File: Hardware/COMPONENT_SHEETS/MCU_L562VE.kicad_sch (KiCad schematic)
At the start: 31 parts, among them SW1 MCU Reset, U2 STM32L562VET6Q, Y1 32MHz

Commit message: Routed Alert I2C lines
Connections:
- net I2C2_EN: now reaches U2.43 (PE15)
- no-connect marks 59 -> 58
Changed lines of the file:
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@@
   (no_connect (at 77.47 60.96))
   (no_connect (at 77.47 119.38))
-  (no_connect (at 77.47 121.92))
   (no_connect (at 123.19 162.56))
   (no_connect (at 77.47 48.26))
@@
   (no_connect (at 123.19 88.9))
   (no_connect (at 123.19 83.82))
+  (no_connect (at 77.47 111.76))
   (no_connect (at 77.47 104.14))
   (no_connect (at 77.47 106.68))
   (no_connect (at 77.47 109.22))
-  (no_connect (at 77.47 111.76))
   (no_connect (at 123.19 50.8))
   (no_connect (at 123.19 93.98))
@@
     (effects (font (size 1.27 1.27)) (justify left))
   )
+  (hierarchical_label "I2C2_EN" (shape input) (at 77.47 121.92 180)
+    (effects (font (size 1.27 1.27)) (justify right))
+  )
   (hierarchical_label "ABORT_2" (shape input) (at 123.19 106.68 0)

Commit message: All traces routed
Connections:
- net at U2.38 (PE10): now also D1.2 (A)
- net at U2.39 (PE11): now also D2.2 (A)
- net at U2.40 (PE12): now also D3.2 (A)
- net at U2.41 (PE13): now also D4.2 (A)
- net at U2.42 (PE14): now also D5.2 (A)
- no-connect marks 58 -> 53
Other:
- moved on the sheet: D1, D2, D3, D4, D5, R17, R18, R19, R20, R21

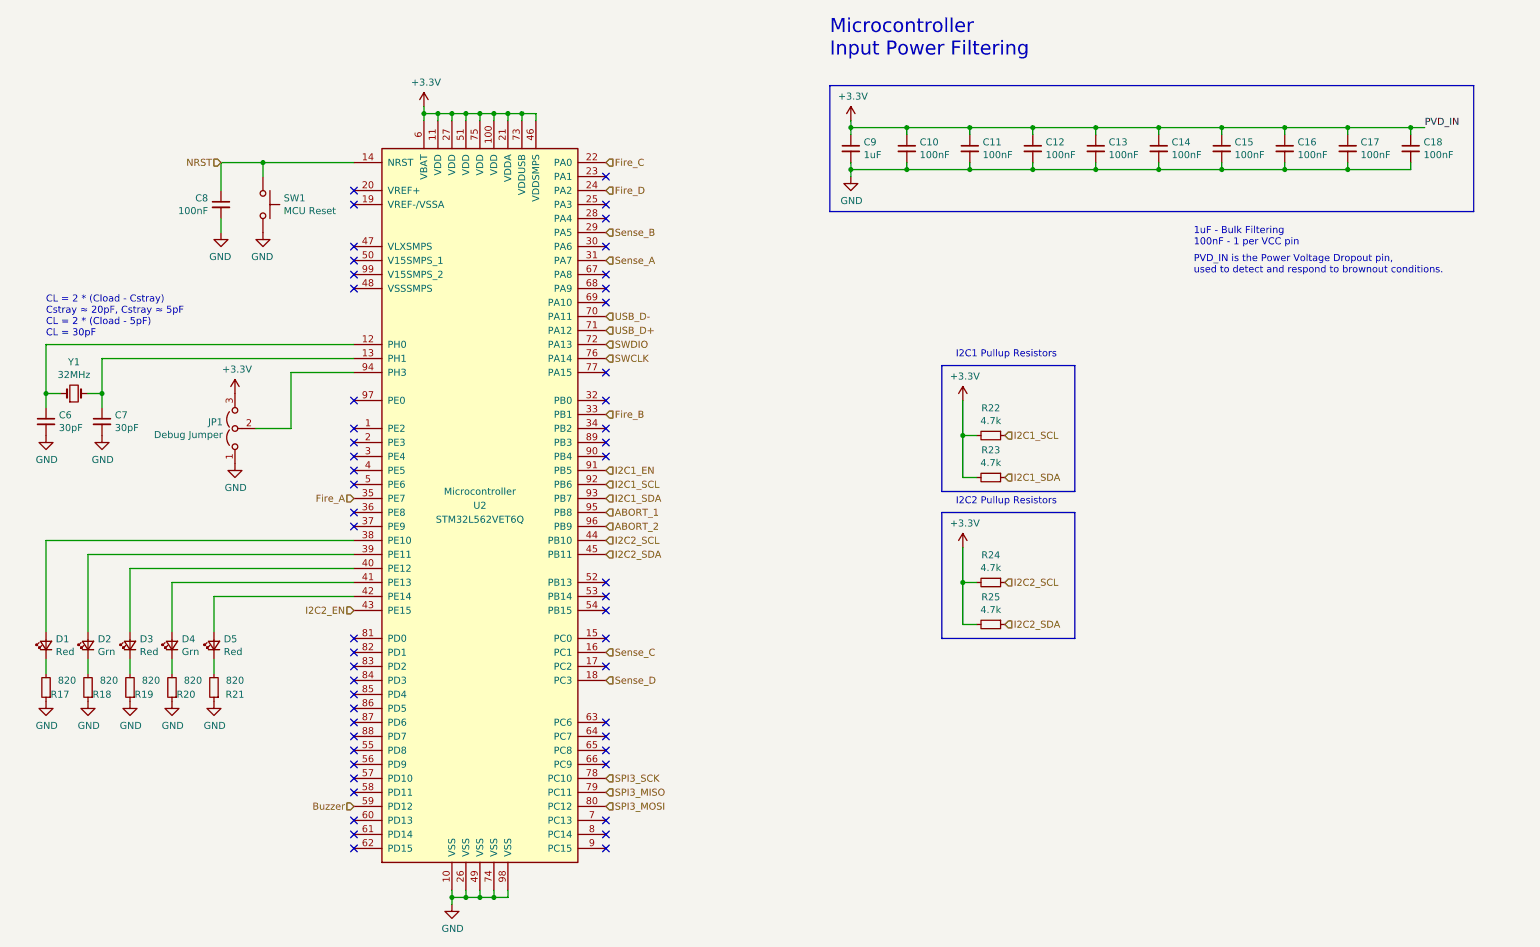
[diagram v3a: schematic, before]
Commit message: Adjusted silkscreen labels, corrected MCU pinout, added pull up resistor to bootloader line, added usb cut out
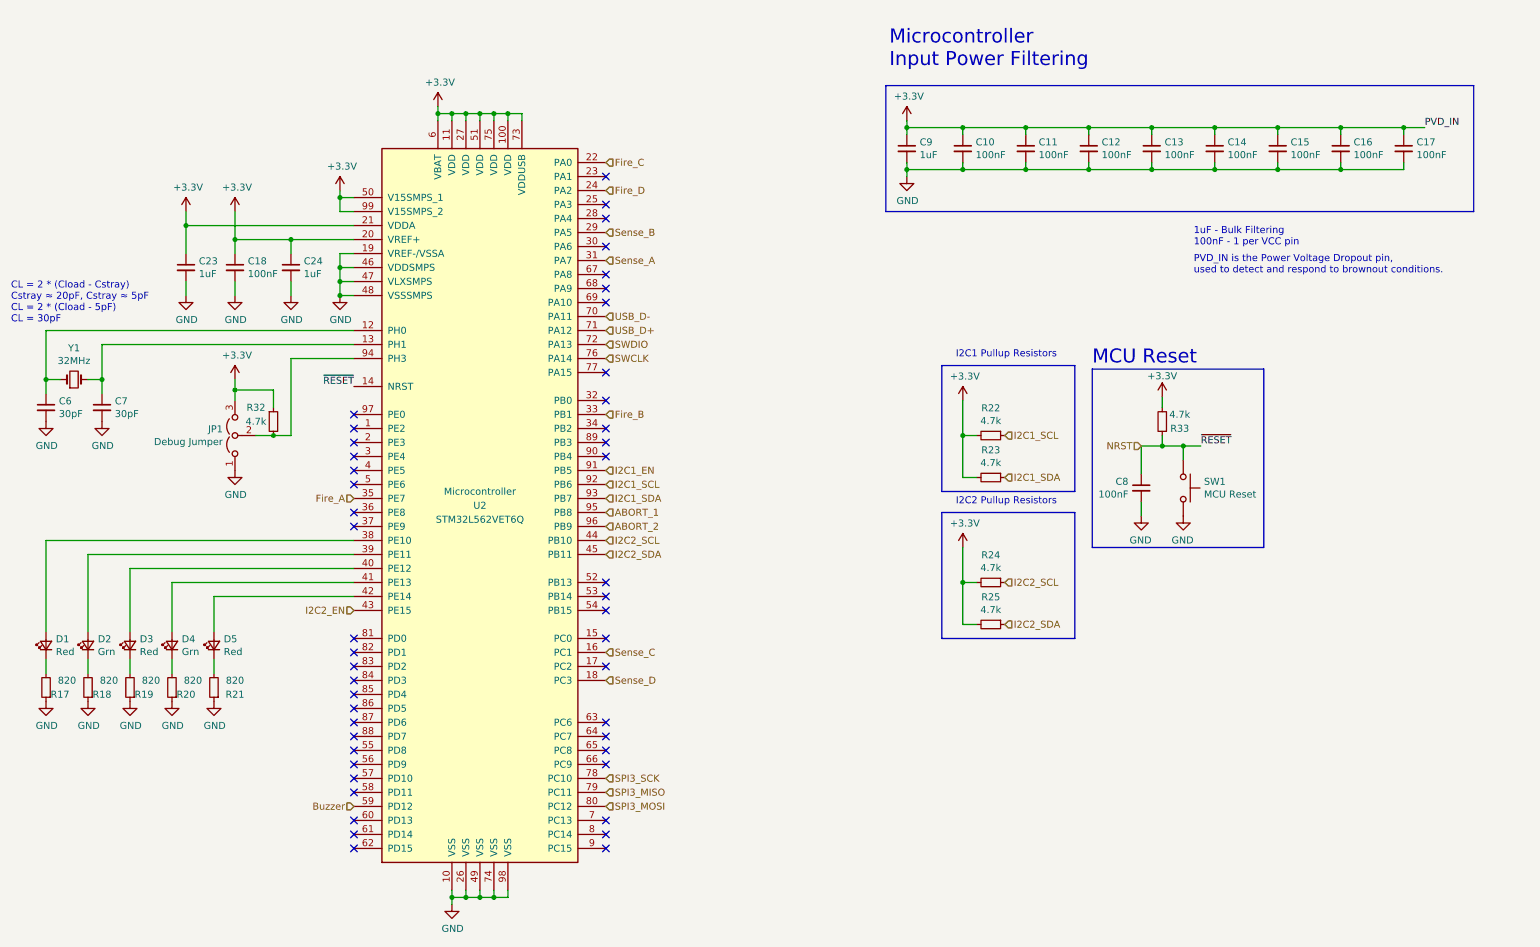
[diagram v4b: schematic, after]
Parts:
- added C23, C24: 1uF, Capacitor_SMD:C_0603_1608Metric_Pad1.08x0.95mm_HandSolder, symbol Device:C_Small
- added R32: 4.7k, Resistor_SMD:R_0603_1608Metric_Pad0.98x0.95mm_HandSolder, symbol Device:R_Small
- added R33: 4.7k, Resistor_SMD:R_0603_1608Metric_Pad1.05x0.95mm_HandSolder, symbol Device:R_Small
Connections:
- net +3V3: now also U2.20 (VREF+), U2.50 (V15SMPS_1), U2.99 (V15SMPS_2), C23.1, C24.1, R32.1, R33.2; no longer U2.46 (VDDSMPS)
- net GND: now also U2.19 (VREF-/VSSA), U2.46 (VDDSMPS), U2.47 (VLXSMPS), U2.48 (VSSSMPS), C23.2, C24.2
- net NRST: now also R33.1
- net at JP1.2 (C), U2.94 (PH3): now also R32.2
- no-connect marks 53 -> 47
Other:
- note added: "MCU Reset"
- moved on the sheet: C10, C11, C12, C13, C14, C15, C16, C17, C6, C7, C9, JP1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
